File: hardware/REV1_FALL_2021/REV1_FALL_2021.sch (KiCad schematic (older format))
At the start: 22 parts, among them J101 Screw_Terminal_01x02, Q101 Q_NMOS_GDS, U1 Teensy3.6_All_Pins, U2 PA16165_Breakout, U3 MPL3115A2_Breakout, U4 BNO055_Breakout, U5 RFM69HCW_Breakout

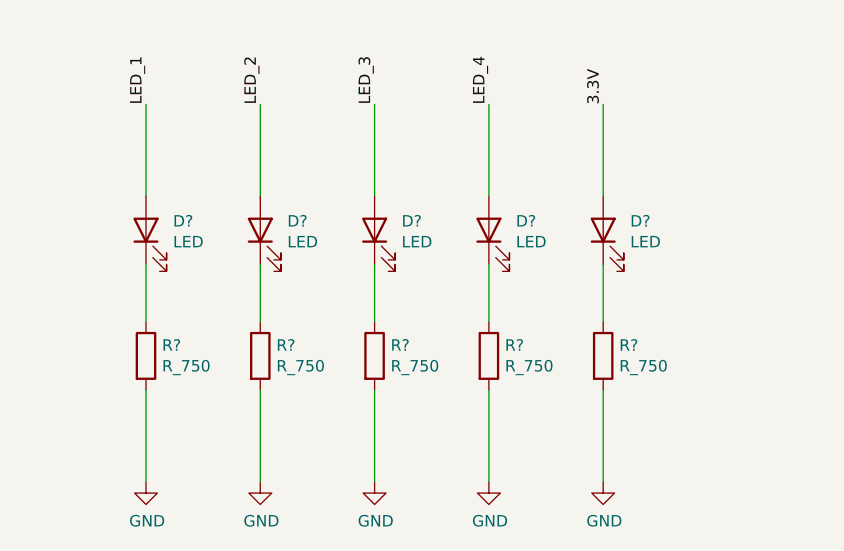
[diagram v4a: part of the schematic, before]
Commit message: add LEDs to layout
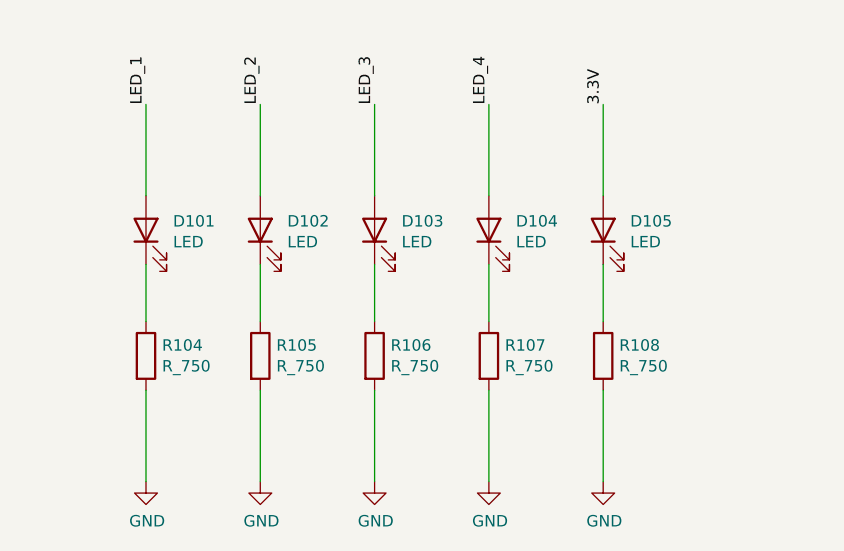
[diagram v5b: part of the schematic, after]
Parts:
- gave numbers to parts that had none: 10
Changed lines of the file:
@@
 Connection ~ 2050 6900
 $Comp
-L Device:LED D?
+L Device:LED D101
 U 1 1 619C7C94
 P 1200 8950
-F 0 "D?" V 1239 8832 50  0000 R CNN
+F 0 "D101" V 1239 8832 50  0000 R CNN
 F 1 "LED" V 1148 8832 50  0000 R CNN
 F 2 "LED_SMD:LED_0805_2012Metric_Pad1.15x1.40mm_HandSolder" H 1200 8950 50  0001 C CNN
@@
 $EndComp
 $Comp
-L Device:R R?
+L Device:R R104
 U 1 1 619CBBB6
 P 1200 9500
-F 0 "R?" H 1270 9546 50  0000 L CNN
+F 0 "R104" H 1270 9546 50  0000 L CNN
 F 1 "R_750" H 1270 9455 50  0000 L CNN
 F 2 "Resistor_SMD:R_0805_2012Metric_Pad1.20x1.40mm_HandSolder" V 1130 9500 50  0001 C CNN
@@
 	1200 9650 1200 10050
 $Comp
-L power:GND #PWR?
+L power:GND #PWR0102
 U 1 1 619E5D47
 P 1200 10050
-F 0 "#PWR?" H 1200 9800 50  0001 C CNN
+F 0 "#PWR0102" H 1200 9800 50  0001 C CNN
 F 1 "GND" H 1205 9877 50  0000 C CNN
 F 2 "" H 1200 10050 50  0001 C CNN
@@
 $EndComp
 $Comp
-L Device:LED D?
+L Device:LED D102
 U 1 1 619E9614
 P 1700 8950
-F 0 "D?" V 1739 8832 50  0000 R CNN
+F 0 "D102" V 1739 8832 50  0000 R CNN
 F 1 "LED" V 1648 8832 50  0000 R CNN
 F 2 "LED_SMD:LED_0805_2012Metric_Pad1.15x1.40mm_HandSolder" H 1700 8950 50  0001 C CNN
@@
 $EndComp
 $Comp
-L Device:R R?
+L Device:R R105
 U 1 1 619E961A
 P 1700 9500
-F 0 "R?" H 1770 9546 50  0000 L CNN
+F 0 "R105" H 1770 9546 50  0000 L CNN
 F 1 "R_750" H 1770 9455 50  0000 L CNN
 F 2 "Resistor_SMD:R_0805_2012Metric_Pad1.20x1.40mm_HandSolder" V 1630 9500 50  0001 C CNN
@@
 	1700 9650 1700 10050
 $Comp
-L power:GND #PWR?
+L power:GND #PWR0103
 U 1 1 619E9624
 P 1700 10050
-F 0 "#PWR?" H 1700 9800 50  0001 C CNN
+F 0 "#PWR0103" H 1700 9800 50  0001 C CNN
 F 1 "GND" H 1705 9877 50  0000 C CNN
 F 2 "" H 1700 10050 50  0001 C CNN
@@
 $EndComp
 $Comp
-L Device:LED D?
+L Device:LED D103
 U 1 1 619EBAF0
 P 2200 8950
-F 0 "D?" V 2239 8832 50  0000 R CNN
+F 0 "D103" V 2239 8832 50  0000 R CNN
 F 1 "LED" V 2148 8832 50  0000 R CNN
 F 2 "LED_SMD:LED_0805_2012Metric_Pad1.15x1.40mm_HandSolder" H 2200 8950 50  0001 C CNN
@@
 $EndComp
 $Comp
-L Device:R R?
+L Device:R R106
 U 1 1 619EBAF6
 P 2200 9500
-F 0 "R?" H 2270 9546 50  0000 L CNN
+F 0 "R106" H 2270 9546 50  0000 L CNN
 F 1 "R_750" H 2270 9455 50  0000 L CNN
 F 2 "Resistor_SMD:R_0805_2012Metric_Pad1.20x1.40mm_HandSolder" V 2130 9500 50  0001 C CNN
@@
 	2200 9650 2200 10050
 $Comp
-L power:GND #PWR?
+L power:GND #PWR0104
 U 1 1 619EBB00
 P 2200 10050
-F 0 "#PWR?" H 2200 9800 50  0001 C CNN
+F 0 "#PWR0104" H 2200 9800 50  0001 C CNN
 F 1 "GND" H 2205 9877 50  0000 C CNN
 F 2 "" H 2200 10050 50  0001 C CNN
@@
 $EndComp
 $Comp
-L Device:LED D?
+L Device:LED D104
 U 1 1 619EE1C7
 P 2700 8950
-F 0 "D?" V 2739 8832 50  0000 R CNN
+F 0 "D104" V 2739 8832 50  0000 R CNN
 F 1 "LED" V 2648 8832 50  0000 R CNN
 F 2 "LED_SMD:LED_0805_2012Metric_Pad1.15x1.40mm_HandSolder" H 2700 8950 50  0001 C CNN
@@
 $EndComp
 $Comp
-L Device:R R?
+L Device:R R107
 U 1 1 619EE1CD
 P 2700 9500
-F 0 "R?" H 2770 9546 50  0000 L CNN
+F 0 "R107" H 2770 9546 50  0000 L CNN
 F 1 "R_750" H 2770 9455 50  0000 L CNN
 F 2 "Resistor_SMD:R_0805_2012Metric_Pad1.20x1.40mm_HandSolder" V 2630 9500 50  0001 C CNN
@@
 	2700 9650 2700 10050
 $Comp
-L power:GND #PWR?
+L power:GND #PWR0105
 U 1 1 619EE1D7
 P 2700 10050
-F 0 "#PWR?" H 2700 9800 50  0001 C CNN
+F 0 "#PWR0105" H 2700 9800 50  0001 C CNN
 F 1 "GND" H 2705 9877 50  0000 C CNN
 F 2 "" H 2700 10050 50  0001 C CNN
@@
 $EndComp
 $Comp
-L Device:LED D?
+L Device:LED D105
 U 1 1 619F098B
 P 3200 8950
-F 0 "D?" V 3239 8832 50  0000 R CNN
+F 0 "D105" V 3239 8832 50  0000 R CNN
 F 1 "LED" V 3148 8832 50  0000 R CNN
 F 2 "LED_SMD:LED_0805_2012Metric_Pad1.15x1.40mm_HandSolder" H 3200 8950 50  0001 C CNN
@@
 $EndComp
 $Comp
-L Device:R R?
+L Device:R R108
 U 1 1 619F0991
 P 3200 9500
-F 0 "R?" H 3270 9546 50  0000 L CNN
+F 0 "R108" H 3270 9546 50  0000 L CNN
 F 1 "R_750" H 3270 9455 50  0000 L CNN
 F 2 "Resistor_SMD:R_0805_2012Metric_Pad1.20x1.40mm_HandSolder" V 3130 9500 50  0001 C CNN
@@
 	3200 9650 3200 10050
 $Comp
-L power:GND #PWR?
+L power:GND #PWR0106
 U 1 1 619F099B
 P 3200 10050
-F 0 "#PWR?" H 3200 9800 50  0001 C CNN
+F 0 "#PWR0106" H 3200 9800 50  0001 C CNN
 F 1 "GND" H 3205 9877 50  0000 C CNN
 F 2 "" H 3200 10050 50  0001 C CNN
